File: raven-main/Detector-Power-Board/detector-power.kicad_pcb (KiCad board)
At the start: 2 copper layers, 37 x 52.5 mm, 28 parts, among them J1 DeployLipo, J2 Conn_01x06, J9 UCLipo, U1 LT8330IS6-TRMPBF, U7 TPS7A4701xRGW, U8 TPS7A4701xRGW

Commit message: Added LDO on 25V rail
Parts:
- added C48: 10uF, Capacitor_SMD:C_0805_2012Metric, F.Cu at (130.6, 104.1)
- added C49: 1uF, Capacitor_SMD:C_0805_2012Metric, F.Cu at (126.7, 100.6)
- added C50: 47uF, Capacitor_SMD:C_0805_2012Metric, F.Cu at (135.6, 104.1)
- added R40: 167k, Resistor_SMD:R_0402_1005Metric, F.Cu at (138.2, 99.3)
- added R41: 10k, Resistor_SMD:R_0402_1005Metric, F.Cu at (138.2, 96.0)
- added U9: TPS7A4701xRGW, Package_DFN_QFN:Texas_RGW0020A_VQFN-20-1EP_5x5mm_P0.65mm_EP3.15x3.15mm_ThermalVias, F.Cu at (132.8, 98.6)
- moved R38 1.27 mm to (129.0, 78.5), turned to -90 degrees
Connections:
- J2 pad 1: /Power_Out_25V -> /Filtered_Power_Out_25V
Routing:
- net /Filtered_Power_Out_25V: track 0.00 -> 25.5 mm
- net GND: track 167.8 -> 192.8 mm, vias 5 -> 12
- net /ON-OFF: track 42.3 -> 58.7 mm, vias 5 -> 6
- net /Power_Out_25V: track 28.3 -> 34.3 mm, vias 0 -> 2
- net Net-(U9-SENSE/FB): track 0.00 -> 5.36 mm
- net Net-(U9-NR): track 0.00 -> 3.85 mm
- net /Data_Out_3V3: track 20.0 -> 18.8 mm
- net Net-(U8-SENSE/FB): track 9.12 -> 8.34 mm

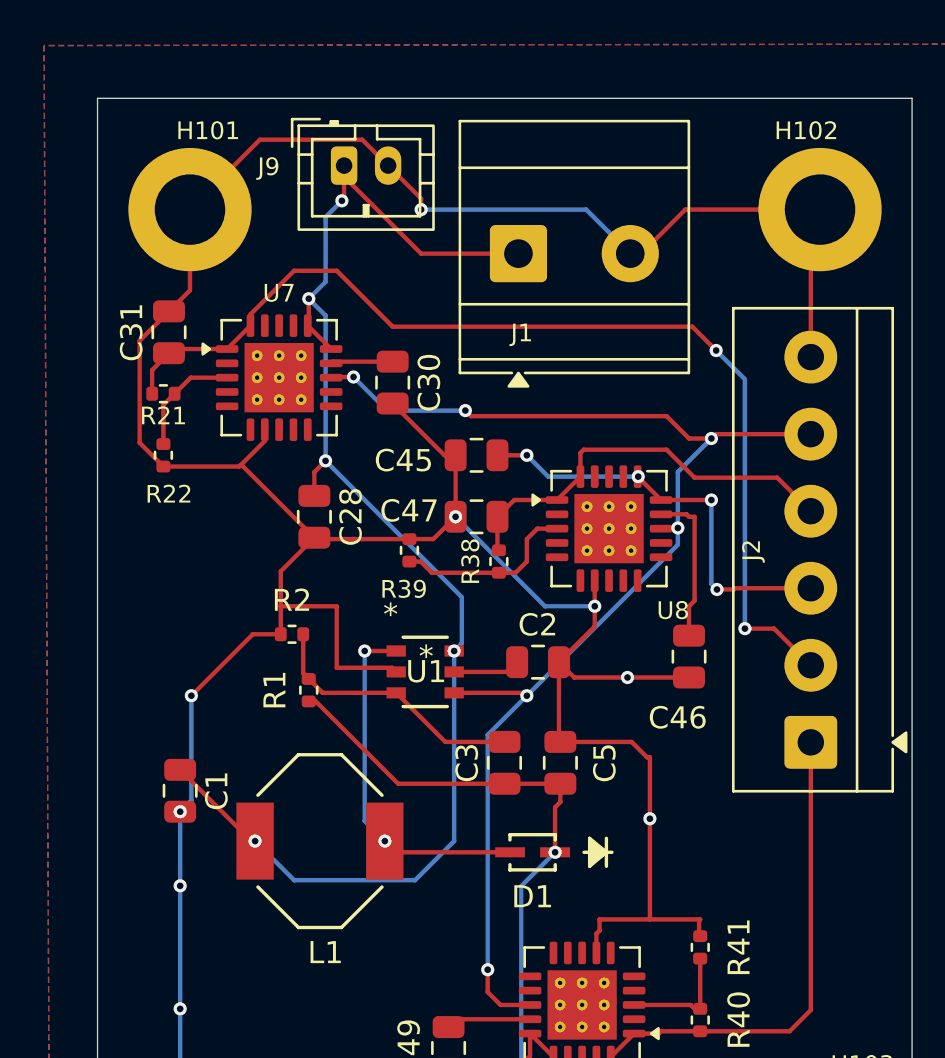
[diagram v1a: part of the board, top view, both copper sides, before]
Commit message: Fixed labels and zones
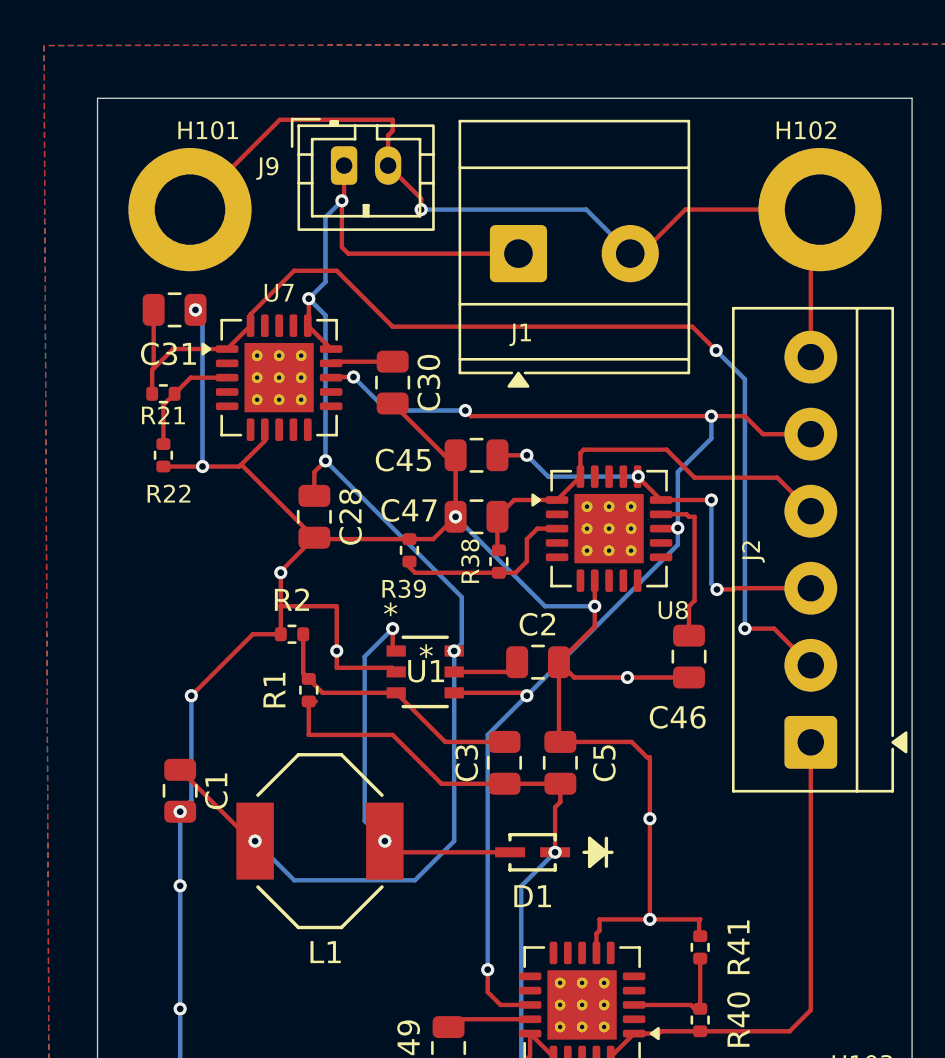
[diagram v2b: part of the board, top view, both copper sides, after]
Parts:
- R1: value 147k -> 162k
- moved C31 1.05 mm to (114.3, 67.1), turned to 0 degrees
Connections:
- net /Power_Out_25V renamed /Power_Out_27.5V
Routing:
- net GND: track 192.8 -> 189.6 mm, vias 12 -> 17
- net /Power_Out_5V: track 47.2 -> 49.9 mm
- net /Power_Out_27.5V: track 34.3 -> 35.5 mm
- net Net-(D1-A): track 16.3 -> 17.5 mm
- net /BBIN: track 64.1 -> 65.0 mm
- net /ON-OFF: track 58.7 -> 59.5 mm

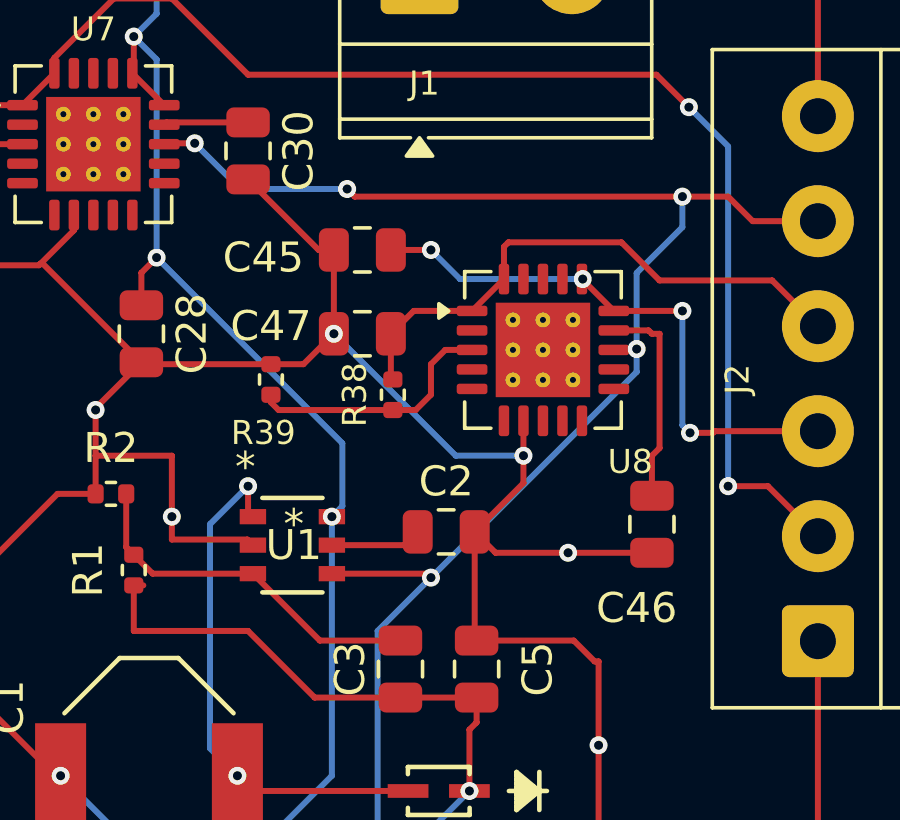
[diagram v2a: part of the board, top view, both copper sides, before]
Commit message: Added 3.3V voltage divider to detector board
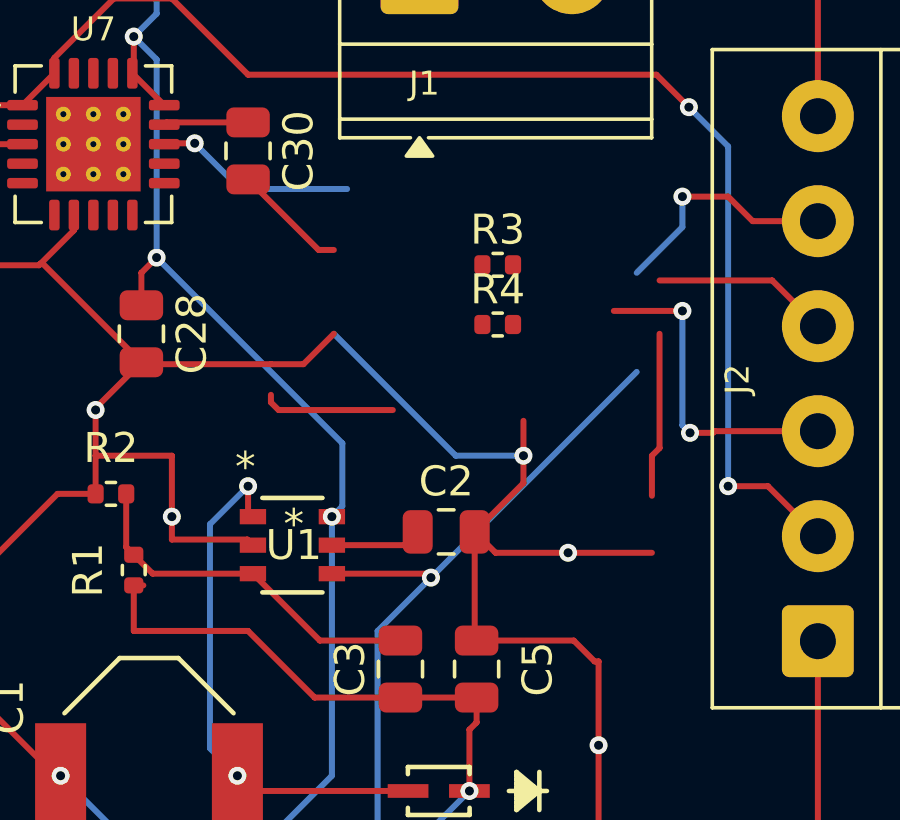
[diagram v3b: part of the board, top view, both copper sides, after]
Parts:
- removed C45: 10uF, Capacitor_SMD:C_0805_2012Metric
- removed C46: 1uF, Capacitor_SMD:C_0805_2012Metric
- removed C47: 47uF, Capacitor_SMD:C_0805_2012Metric
- removed R38: 13.3k, Resistor_SMD:R_0402_1005Metric
- removed R39: 9.76k, Resistor_SMD:R_0402_1005Metric
- removed U8: TPS7A4701xRGW, Package_DFN_QFN:Texas_RGW0020A_VQFN-20-1EP_5x5mm_P0.65mm_EP3.15x3.15mm_ThermalVias
- added R3: 5.2k, Resistor_SMD:R_0402_1005Metric, F.Cu at (132.5, 74.2)
- added R4: 10k, Resistor_SMD:R_0402_1005Metric, F.Cu at (132.5, 76.1)
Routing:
- net /ON-OFF: track 59.5 -> 44.2 mm, vias 6 -> 4
- net /Data_Out_3V3: track 18.8 -> 5.91 mm
- net (no net): track 0.00 -> 9.93 mm
- net Net-(U8-SENSE/FB): track 8.49 -> 0.00 mm
- net /Data_In_5V: track 19.0 -> 10.7 mm, vias 4 -> 2
- net Net-(U8-NR): track 7.08 -> 0.00 mm
- net GND: track 189.6 -> 186.8 mm, vias 17 -> 16

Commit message: Redesigned power board (again!)
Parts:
- removed C28, C48: 10uF, Capacitor_SMD:C_0805_2012Metric
- removed C30, C49: 1uF, Capacitor_SMD:C_0805_2012Metric
- removed C31, C50: 47uF, Capacitor_SMD:C_0805_2012Metric
- removed R21: 25.5k, Resistor_SMD:R_0402_1005Metric
- removed R22: 9.76k, Resistor_SMD:R_0402_1005Metric
- removed R40: 167k, Resistor_SMD:R_0402_1005Metric
- removed R41: 10k, Resistor_SMD:R_0402_1005Metric
- removed U7, U9: TPS7A4701xRGW, Package_DFN_QFN:Texas_RGW0020A_VQFN-20-1EP_5x5mm_P0.65mm_EP3.15x3.15mm_ThermalVias
- added C10: 1u, Capacitor_SMD:C_0805_2012Metric, F.Cu at (130.0, 91.4)
- added C11: 1n, Capacitor_SMD:C_0805_2012Metric, F.Cu at (120.7, 72.1)
- added C12: 5u, Capacitor_SMD:C_0805_2012Metric, F.Cu at (120.4, 65.3)
- added C4: 0.1u, Capacitor_SMD:C_0805_2012Metric, F.Cu at (114.6, 80.3)
- added C6: 0.1u, Capacitor_SMD:C_0805_2012Metric, F.Cu at (122.2, 104.1)
- added C7: 1u, Capacitor_SMD:C_0805_2012Metric, F.Cu at (127.0, 81.0)
- added C8: 1u, Capacitor_SMD:C_0805_2012Metric, F.Cu at (143.8, 99.3)
- added C9: 1u, Capacitor_SMD:C_0805_2012Metric, F.Cu at (130.3, 75.4)
- added D3: 1N4002, Diode_THT:D_DO-41_SOD81_P10.16mm_Horizontal, F.Cu at (135.6, 76.2)
- added D4: 1N4002, Diode_THT:D_DO-41_SOD81_P10.16mm_Horizontal, F.Cu at (114.6, 94.2)
- added D5: 1N4002, Diode_THT:D_DO-41_SOD81_P10.16mm_Horizontal, F.Cu at (120.4, 98.8)
- added D6: 1N4002, Diode_THT:D_DO-41_SOD81_P10.16mm_Horizontal, F.Cu at (137.2, 104.1)
- added R5: 4.56k, Resistor_SMD:R_0402_1005Metric, F.Cu at (106.4, 42.4)
- added R6: 240, Resistor_SMD:R_0402_1005Metric, F.Cu at (143.0, 94.5)
- added R7: 720, Resistor_SMD:R_0402_1005Metric, F.Cu at (106.4, 46.4)
- added R8: R_Variable, Resistor_SMD:R_0805_2012Metric, F.Cu at (126.0, 91.4)
- added U2: TPS22810DRV, Package_SON:WSON-6-1EP_2x2mm_P0.65mm_EP1x1.6mm, F.Cu at (120.4, 69.0)
- added U3: LM317LCLPRE3, LM317AMDTNOPB:TD03B_TEX, F.Cu at (121.7, 81.0)
- added U4: LM317LCLPRE3, LM317AMDTNOPB:TD03B_TEX, F.Cu at (137.4, 94.5)
- J2: value Conn_01x06 -> Conn_01x04; footprint TerminalBlock_4Ucon:TerminalBlock_4Ucon_1x06_P3.50mm_Horizontal -> Connector_PinHeader_2.54mm:PinHeader_1x04_P2.54mm_Vertical
- R3: value 5.2k -> 240
- R4: value 10k -> R_Variable; footprint Resistor_SMD:R_0402_1005Metric -> Resistor_SMD:R_0805_2012Metric
- moved J2 34.0 mm to (114.8, 68.1), turned to 0 degrees
- moved C1 31.3 mm to (144.5, 79.8)
- moved L1 28.3 mm to (142.5, 72.9), turned to 90 degrees
- moved R2 20.7 mm to (140.2, 83.6), turned to 0 degrees
- moved R1 19.9 mm to (140.2, 85.6), turned to 180 degrees
- moved D1 19.5 mm to (135.6, 72.9), turned to 0 degrees
- moved R4 19.4 mm to (120.7, 91.4)
- moved U1 15.4 mm to (140.8, 80.5)
- moved C5 13.5 mm to (145.3, 88.6), turned to -90 degrees
- moved C2 13.2 mm to (144.0, 84.1), turned to -90 degrees
- moved R3 12.0 mm to (126.5, 84.6), turned to 90 degrees
- moved C3 11.2 mm to (140.5, 87.9), turned to 180 degrees
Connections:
- C2 pad 1: Net-(U1-INTVCC) -> Net-(U1-EN/UVLO)
- J1 pad 1: /BBIN -> Net-(J1-Pin_1)
- J2 pad 3: /Data_In_5V -> /ON-OFF
- J2 pad 4: /Data_Out_3V3 -> GND
- J9 pad 1: /BBIN -> Net-(J1-Pin_1)
- R3 pad 1: /Data_In_5V -> Net-(D3-A)
- R3 pad 2: /Data_Out_3V3 -> /Power_Out_5V
- R4 pad 1: /Data_Out_3V3 -> GND
- R4 pad 2: GND -> Net-(D3-A)
- U1 pad 4: /ON-OFF -> Net-(U1-EN/UVLO)
- U1 pad 5: Net-(U1-INTVCC) -> Net-(U1-EN/UVLO)
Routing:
- net GND: track 186.8 -> 0.00 mm, vias 16 -> 0
- net /BBIN: track 65.0 -> 0.00 mm, vias 5 -> 0
- net /Power_Out_5V: track 49.9 -> 0.00 mm, vias 2 -> 0
- net /ON-OFF: track 44.2 -> 0.00 mm, vias 4 -> 0
- net /Power_Out_27.5V: track 35.5 -> 0.00 mm, vias 2 -> 0
- net /Filtered_Power_Out_25V: track 25.5 -> 0.00 mm
- net Net-(D1-A): track 17.5 -> 0.00 mm, vias 2 -> 0
- net Net-(U1-FBX): track 12.2 -> 0.00 mm
- net /Data_In_5V: track 10.7 -> 0.00 mm, vias 2 -> 0
- net (no net): track 9.93 -> 0.00 mm
- net /Data_Out_3V3: track 5.91 -> 0.00 mm
- net Net-(U9-SENSE/FB): track 5.36 -> 0.00 mm
- net Net-(U7-SENSE/FB): track 5.18 -> 0.00 mm
- net Net-(U9-NR): track 3.85 -> 0.00 mm
- net Net-(U1-INTVCC): track 3.04 -> 0.00 mm
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
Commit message: Laid out tracks
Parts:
- moved D5 10.9 mm to (131.1, 101.1), turned to 90 degrees
- moved D6 9.16 mm to (128.0, 104.6), turned to 0 degrees
- moved C10 7.38 mm to (123.4, 94.7)
- moved D3 4.85 mm to (130.8, 76.7)
- moved C9 3.95 mm to (127.5, 72.6)
- moved C5 2.90 mm to (142.5, 87.9)
- moved C3 2.81 mm to (137.7, 87.6)
- moved D1 2.29 mm to (135.6, 75.2)
- moved R8 1.98 mm to (124.7, 89.9)
- moved R1 1.61 mm to (138.7, 85.1)
- moved R2 1.55 mm to (138.7, 83.3)
- moved U1 1.52 mm to (139.2, 80.5)
- moved U3 1.30 mm to (121.4, 79.8)
- moved C8 0.92 mm to (144.5, 98.8), turned to 90 degrees
- moved C1 0.80 mm to (143.8, 79.5)
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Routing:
- net /Filtered_Power_Out_25V: track 0.00 -> 72.4 mm, vias 0 -> 2
- net /BBIN: track 0.00 -> 66.7 mm, vias 0 -> 6
- net /Power_Out_27.5V: track 0.00 -> 51.2 mm, vias 0 -> 2
- net Net-(D6-A): track 0.00 -> 49.0 mm, vias 0 -> 1
- net /Power_Out_5V: track 0.00 -> 41.0 mm, vias 0 -> 2
- net Net-(D3-A): track 0.00 -> 27.4 mm, vias 0 -> 2
- net Net-(J1-Pin_1): track 0.00 -> 17.0 mm
- net Net-(D1-A): track 0.00 -> 14.2 mm
- net /ON-OFF: track 0.00 -> 12.1 mm, vias 0 -> 2
- net Net-(U1-FBX): track 0.00 -> 6.94 mm
- net Net-(U1-EN/UVLO): track 0.00 -> 4.41 mm
- net Net-(U2-CT): track 0.00 -> 2.59 mm
- net Net-(U2-GND-Pad4): track 0.00 -> 1.16 mm
